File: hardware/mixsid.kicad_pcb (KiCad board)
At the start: 2 copper layers, 62.2 x 57.4 mm, 76 parts, among them P1 INPUT, P2 CONTROL, P3 RAW, P4 SOCKET LEFT, P5 OUTPUT, P6 SOCKET RIGHT, Q1 BC547, Q2 BC547, U1 GAL16V8, U2 SID2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

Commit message: MixSID_SMD
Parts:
- C1, C10, C11, C12, C13, C14, C15, C16, C2, C20, C21, C23, C24, C25, C26, C27, C3, C4, C5, C6, C7, C8, C9: footprint Pinheaders:C_Disc_D3_P2.5 -> Pinheaders:0805
- C17, C18, C19, C22: footprint Pinheaders:C_Radial_D5_L6_P2.5 -> Pinheaders:0805
- D1, D2: value 1N4002 -> S1A; footprint Discret:DO-41 -> Pinheaders:DO-214AC
- JP1, JP12, JP2, JP8: footprint Pinheaders:Pin_Header_Straight_1x03_Pitch2.00mm_Jumper_1-2 -> Pinheaders:Pin_Header_Straight_1x03_Pitch2.00mm
- JP11, JP13, JP5, JP6, JP7: footprint Pinheaders:Pin_Header_Straight_1x03_Pitch2.00mm_Jumper_2-3 -> Pinheaders:Pin_Header_Straight_1x03_Pitch2.00mm
- P1: value INPUT -> INPUT DF13-5P; footprint Pinheaders:Pin_Header_Straight_1x05 -> Pinheaders:DF13-5P
- P5: value OUTPUT -> OUTPUT DF13-3P; footprint Pinheaders:Pin_Header_Straight_1x03 -> Pinheaders:DF13-3P
- Q1, Q2: value BC547 -> BCP54; footprint TO_SOT_Packages_THT:TO-92_Inline_Narrow_Oval -> Package_TO_SOT_SMD:SOT-223
- R1, R10, R11, R12, R13, R14, R2, R4, R5, R6, R7, R8, R9: footprint Pinheaders:R1 -> Pinheaders:0805
- U3, U4: footprint Pinheaders:TO-220 -> Package_TO_SOT_SMD:TO-252-2
- U6, U7: footprint Pinheaders:DIP-16_W7.62mm -> Pinheaders:SOIC-16
- U8: footprint Pinheaders:DIP-8_W7.62mm -> Pinheaders:SOIC-8
- e1: renamed from R3; footprint Pinheaders:R1 -> Pinheaders:0805
- moved C25 19.5 mm to (181.7, 76.3), turned to 90 degrees
- moved R8 18.2 mm to (186.9, 76.7), turned to 0 degrees
- moved Q1 15.1 mm to (184.5, 96.1)
- moved C6 13.2 mm to (171.5, 110.1), turned to 0 degrees
- moved R5 13.0 mm to (182.3, 100.9), turned to 90 degrees
- moved U6 12.5 mm to (185.0, 110.3), turned to 270 degrees
- moved C16 11.4 mm to (183.8, 102.9), turned to 90 degrees
- moved R13 10.8 mm to (175.5, 106.4), turned to 90 degrees
- moved R4 9.72 mm to (178.9, 105.1), turned to 180 degrees
- moved R11 8.78 mm to (175.6, 103.8)
- moved C7 8.05 mm to (148.2, 119.5), turned to 180 degrees
- moved R14 7.44 mm to (175.5, 108.8), turned to 90 degrees
- moved C22 7.21 mm to (180.8, 90.8), turned to 270 degrees
- moved C20 7.20 mm to (177.6, 101.4), turned to 270 degrees
- moved C26 6.77 mm to (139.5, 84.2), turned to 180 degrees
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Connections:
- Q1 pad 1: /+12V -> Net-(C15-Pad1)
- Q1 pad 2: Net-(C15-Pad1) -> /+12V
- Q2 pad 1: /+12V -> Net-(C20-Pad1)
- Q2 pad 2: Net-(C20-Pad1) -> /+12V
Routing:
- net GND: track 339.8 -> 175.9 mm, vias 5 -> 12
- net /S2OUT: track 122.6 -> 74.6 mm, vias 1 -> 2
- net /M1: track 52.8 -> 90.1 mm, vias 0 -> 2
- net /PS: track 94.4 -> 77.2 mm
- net Net-(C16-Pad2): track 14.3 -> 26.8 mm, vias 0 -> 2
- net Net-(C12-Pad1): track 27.0 -> 15.2 mm, vias 0 -> 1
- net /VEE: track 34.4 -> 45.8 mm, vias 0 -> 2
- net Net-(C15-Pad1): track 12.5 -> 23.8 mm
- net /D7: track 23.2 -> 34.0 mm
- net VCC: track 84.4 -> 95.1 mm
- net /MONO_OUT: track 42.2 -> 31.9 mm, vias 0 -> 1
- net /VEXT: track 45.6 -> 55.8 mm, vias 0 -> 2
- net Net-(C21-Pad2): track 15.2 -> 24.4 mm
- net /RIGHT: track 29.9 -> 38.4 mm, vias 0 -> 1
- net Net-(C17-Pad1): track 12.1 -> 4.59 mm
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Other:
- board text added: "MixSID Stereo SID Board Rev.2 ©2021"
- board text removed: "BC547A"
- board text removed: "MixSID Stereo SID Board Rev.1 ©2016 Henning Bekel"
- board text removed: "Testing & Feedback by C0zmo, GI-Joe and GMP"

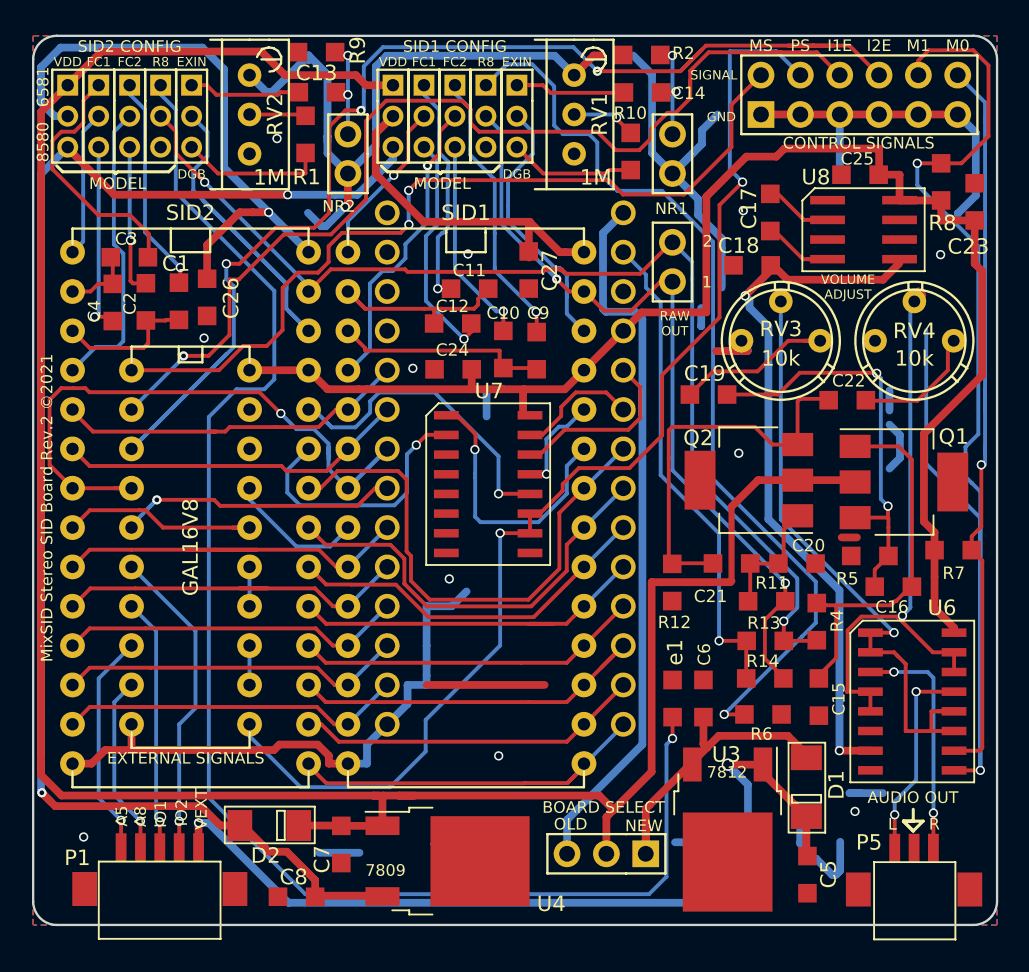
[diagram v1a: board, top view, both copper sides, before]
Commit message: Adjust connectors to match JST GH
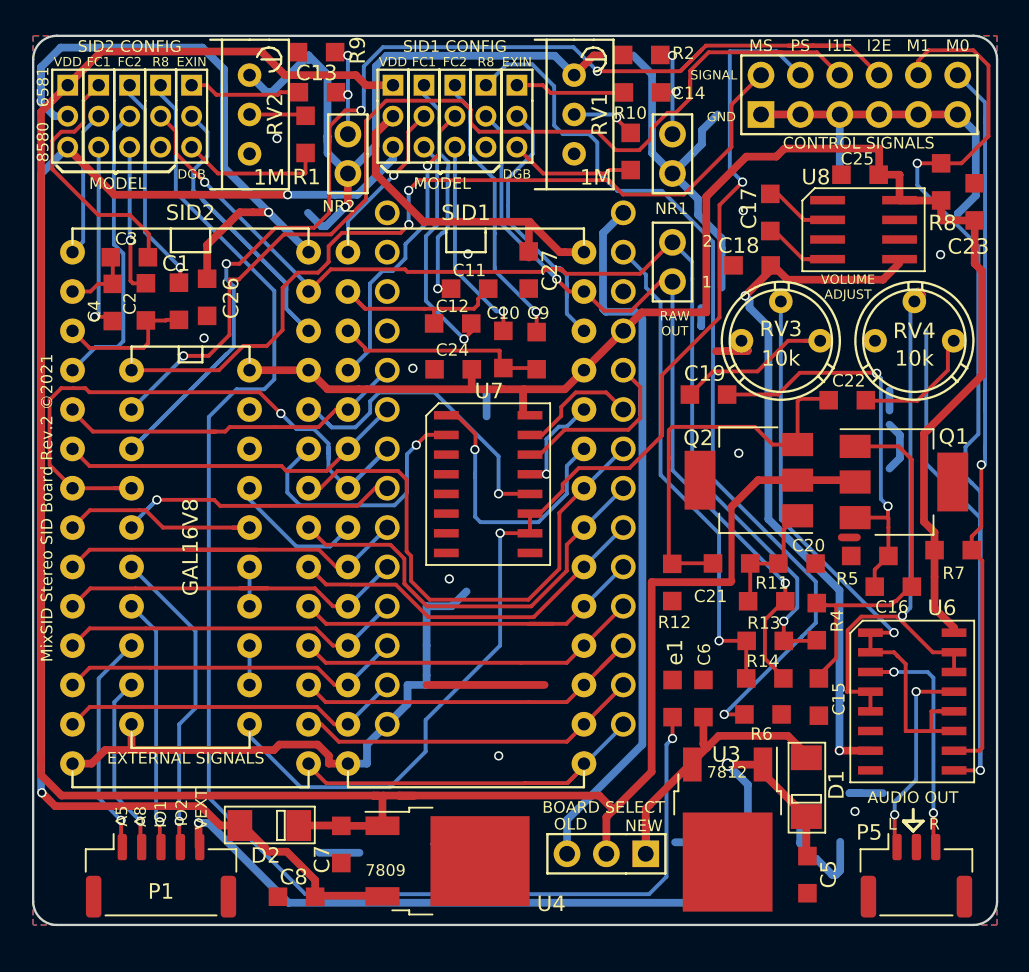
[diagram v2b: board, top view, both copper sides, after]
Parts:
- P1: footprint Pinheaders:DF13-5P -> Connector_JST:JST_GH_SM05B-GHS-TB_1x05-1MP_P1.25mm_Horizontal
- P5: footprint Pinheaders:DF13-3P -> Connector_JST:JST_GH_SM03B-GHS-TB_1x03-1MP_P1.25mm_Horizontal
- moved P5 4.47 mm to (185.3, 121.5)
- moved P1 2.75 mm to (136.5, 121.5)
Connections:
- net /~CS renamed /~{CS}
- net /~CS1 renamed /~{CS1}
- net /~CS2 renamed /~{CS2}
- net /~IO1 renamed /~{IO1}
- net /~IO1EN renamed /~{IO1EN}
- net /~IO2 renamed /~{IO2}
- net /~IO2EN renamed /~{IO2EN}
- net /~RES renamed /~{RES}
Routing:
- net GND: vias 12 -> 11
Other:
- net class Default removed
- net class Power removed
